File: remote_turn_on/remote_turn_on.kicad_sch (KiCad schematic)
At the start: 11 parts, among them J1 SM08B-NSHSS-TB LFSN, U1 ATtiny85-20S, U2 MLX92231LSE

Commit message: Removed neopixel status led and restored dual red/green status led support.
Minor tweaks to RTO pinouts.
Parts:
- R1, R4: value 200 -> 220
- U2: value MLX92231LSE -> MLX92231LSE-AAA-009
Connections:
- net Cam Status +: now also D1.2 (AK), J1.8; no longer D1.1 (KA), J1.7
- net Cam Status -: now also D1.1 (KA), J1.7; no longer D1.2 (AK), J1.8

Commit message: Minor updates to controller, 3rd stab at hadron breakout
Minor updates to controller and firmware to make labels more consistent. Took another try at the hadron IO breakout. Old manufacture files removed.
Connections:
- net Cam Status + renamed Cam Status R
- net Cam Status - renamed Cam Status G
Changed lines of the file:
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@@
 		)
 	)
-	(global_label "Cam Status -"
+	(global_label "Cam Status G"
 		(shape input)
 		(at 76.2 128.27 180)
@@
 		)
 		(property "Intersheetrefs" "${INTERSHEET_REFS}"
-			(at 59.6079 128.27 0)
+			(at 59.9103 128.27 0)
 			(effects
 				(font
@@
 		)
 	)
-	(global_label "Cam Status +"
+	(global_label "Cam Status R"
 		(shape input)
 		(at 76.2 130.81 180)
@@
 		)
 		(property "Intersheetrefs" "${INTERSHEET_REFS}"
-			(at 59.6079 130.81 0)
+			(at 59.9103 130.81 0)
 			(effects
 				(font
@@
 		)
 	)
-	(global_label "Cam Status +"
+	(global_label "Cam Status R"
 		(shape input)
 		(at 152.4 107.95 180)
@@
 		)
 		(property "Intersheetrefs" "${INTERSHEET_REFS}"
-			(at 135.8079 107.95 0)
+			(at 136.1103 107.95 0)
 			(effects
 				(font
@@
 		)
 	)
-	(global_label "Cam Status -"
+	(global_label "Cam Status G"
 		(shape input)
 		(at 167.64 107.95 0)
@@
 		)
 		(property "Intersheetrefs" "${INTERSHEET_REFS}"
-			(at 184.2321 107.95 0)
-			(effects
-				(font
+			(at 183.9297 107.95 0)
+			(effects
+				(font

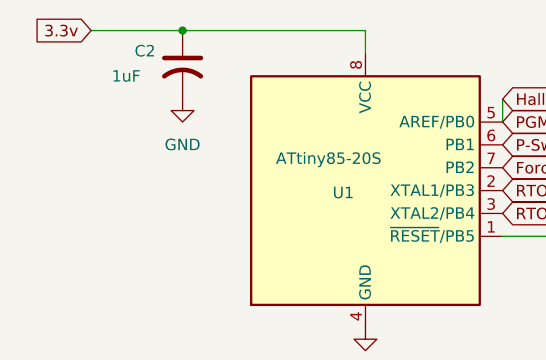
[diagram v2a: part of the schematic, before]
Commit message: Added cutout to controller PCB for HadronDM power connector.
Update also includes v1.2 gerbers - these are now out of date. Current PCB with cutout is version 1.3.
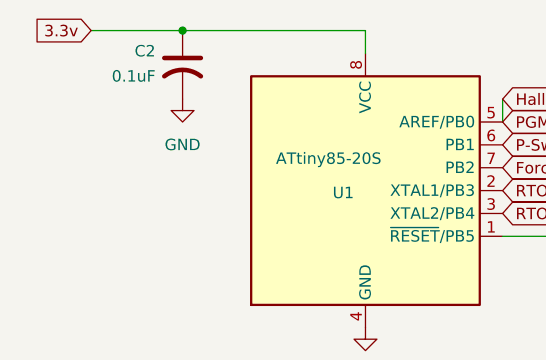
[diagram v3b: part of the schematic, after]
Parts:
- C2: value 1uF -> 0.1uF
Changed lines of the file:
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@@
 			)
 		)
-		(property "Value" "1uF"
+		(property "Value" "0.1uF"
 			(at 61.976 57.15 0)
 			(effects
